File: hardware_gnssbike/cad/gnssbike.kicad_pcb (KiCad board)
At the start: 4 copper layers, 34 x 90 mm, 145 parts, among them J101 HRO TYPE-C-31-M-12, J102 JST SM06B-GHS-TB, J103 JST S4B-ZR-SM4A-TF, J201 Tag-Connect TC2030-NL, J302 Hirose U.FL-R-SMT-1, J401 Hirose FH12-10S-0.5SH(55), J402 HCTL HC-FPC-05-10-5RLTAG, Q401 DMG1012T-7, Q601 DMG1012T-7, Q602 DMG1012T-7, Q603 DMG1012T-7, SW601 XunPu TS-1088R-02026, SW602 XunPu TS-1088R-02026, SW603 XunPu TS-1088R-02026, U101 nPM1300-QEAA, U102 MAX17262REWL, U103 ADP5091ACPZ-2, U104 TPS7A0218PDQN, U201 MinewSemi ME54BS13, U301 u-blox MAX-F10S, U302 TI TXU0204BQAR, U501 MX25R6435F, U502 Bosch BMP585, U503 Bosch BMI270, U504 Memsic MMC5603NJ, U505 TI OPT3001DNPR

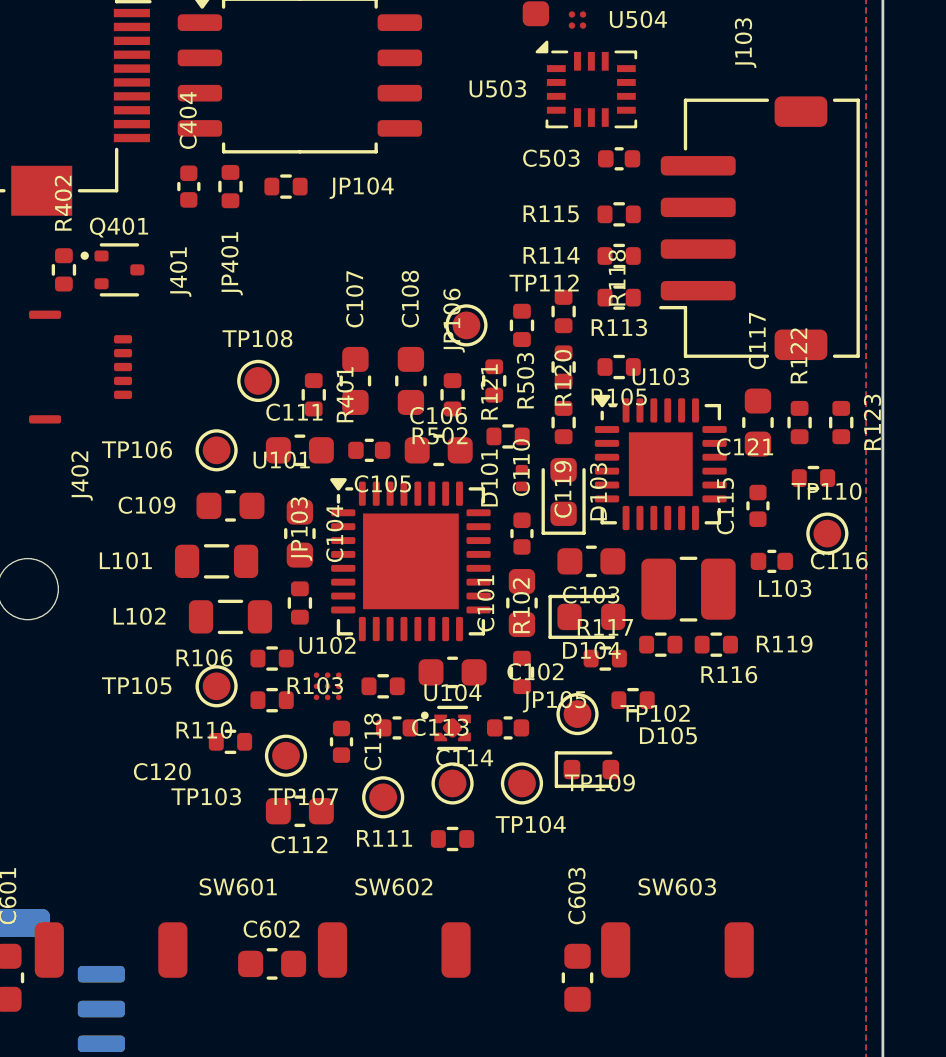
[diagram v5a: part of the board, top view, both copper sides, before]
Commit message: fix(hardware): six pins of the solar harvester were swapped
The second board-killing mistake of the day, and it was caught the same
way as the first: two sources disagreed, and the data sheet decided.

A first reading of the ADP5091 data sheet swapped SIX pins, in two
permutations of three - 2/4/6 (SETHYST, SETSD, TERM) and 7/9/10 (MPPT,
VIN, AGND). It only surfaced because KiCad's own Battery_Management:
ADP5091 symbol disagreed, and because the symbol check had just been
taught to compare pin NAMES and not only numbers. The numbers matched;
the signals did not.

Table 5, pages 8 and 9 of Rev. A (D14145-0-5/17(A)), with Figure 3
confirming side by side, says KiCad is right on all 24. Three
independent readings closed it: the table rebuilt from the geometry of
its columns, the self-consistency of each description - the one for pin
2 says "the SETSD pin", the one for pin 6 says "between SETPG and
SETHYST" - and Figure 3.

What would have gone to copper: the MPPT divider on pin 7, which is
AGND, shorted to analogue ground; the harvester with its 22 uH inductor
and 10 uF capacitor on pin 9, which is MPPT; and ground on pin 10, which
is the input.

The exposed pad is recorded as the data sheet has it: no number at all -
its row in Table 5 has the column empty - and "must be connected to
AGND". The 25 is a CAD convention, which is how KiCad's footprint
numbers it and how its symbol names it, stacked on pin 7.

Beware the preliminary Rev. PrA: its Table 5 swaps 14 and 17 and
contradicts its own Figure 2. It is good for nothing.

With the pinout right, the ADP5091 symbol goes in: 15 KiCad symbols now,
all verified pin number AND pin name.

Verified: check_sch and check_pcb pass, schematic and board agree.
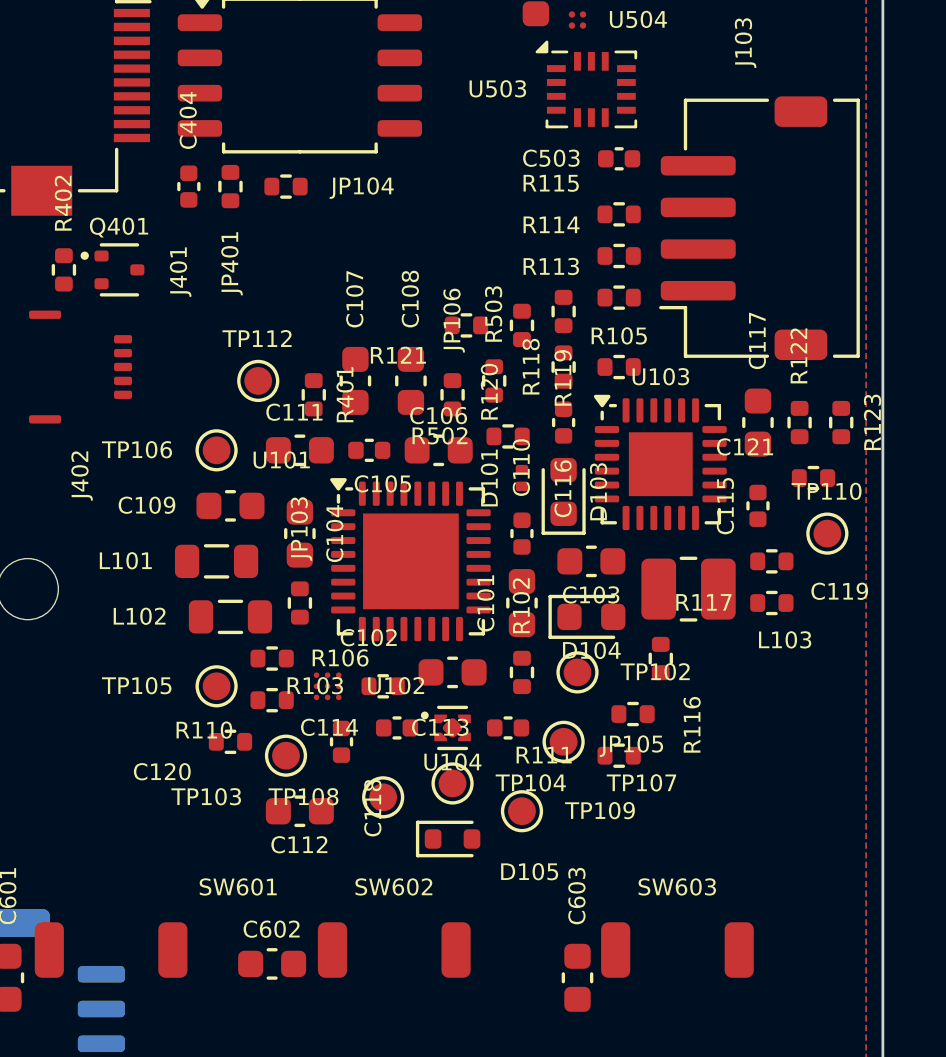
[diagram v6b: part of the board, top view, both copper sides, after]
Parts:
- moved TP108 15.7 mm to (41.0, 77.5)
- moved R119 13.2 mm to (47.5, 60.0), turned to 90 degrees
- moved C116 9.01 mm to (47.5, 64.0), turned to 90 degrees
- moved C119 9.01 mm to (55.0, 69.0), turned to 0 degrees
- moved TP112 7.76 mm to (36.5, 62.5)
- moved TP107 6.80 mm to (47.5, 75.5)
- moved R111 6.71 mm to (49.5, 76.0)
- moved R117 6.32 mm to (55.0, 70.5)
- moved D105 5.59 mm to (43.5, 79.0)
- moved R121 2.00 mm to (44.0, 60.5), turned to 0 degrees
- moved R120 1.58 mm to (46.0, 60.5)
- moved TP102 1.50 mm to (48.0, 73.0)
- moved TP109 1.00 mm to (46.0, 78.0)
- moved JP105 0.50 mm to (50.0, 74.5)
- moved R116 0.50 mm to (51.0, 72.5), turned to 90 degrees
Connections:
- U103 pad 10: GND -> SRC
- U103 pad 2: (no net) -> SETSD
- U103 pad 4: SETSD -> TERM
- U103 pad 6: TERM -> (no net)
- U103 pad 7: MPPT -> GND
- U103 pad 9: SRC -> MPPT
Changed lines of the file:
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@@
 		(at 43.5000 73.0000 0)
 		(property "Reference" "C102"
-			(at 3.0020 0.0000 0)
+			(at -3.0020 -1.2300 0)
 			(layer "F.SilkS")
 			(effects (font (size 0.6 0.6) (thickness 0.12)))
@@
 		(at 41.5000 75.0000 0)
 		(property "Reference" "C114"
-			(at 2.4320 1.1000 0)
+			(at -2.4320 0.0000 0)
 			(layer "F.SilkS")
 			(effects (font (size 0.6 0.6) (thickness 0.12)))
@@
 	(footprint "Capacitor_SMD:C_0402_1005Metric"
 		(layer "F.Cu")
-		(at 55.0000 69.0000 0)
+		(at 47.5000 64.0000 90)
 		(property "Reference" "C116"
-			(at 2.4320 0.0000 0)
+			(at -2.3820 0.0000 90)
 			(layer "F.SilkS")
 			(effects (font (size 0.6 0.6) (thickness 0.12)))
@@
 	)
 	(pad "1" smd roundrect
-		(at -0.48 0)
+		(at -0.48 0 90)
 		(size 0.56 0.62)
 		(layers "F.Cu" "F.Paste" "F.Mask")
@@
 	(pad "2" smd roundrect
 		(net 35 "GND")
-		(at 0.48 0)
+		(at 0.48 0 90)
 		(size 0.56 0.62)
 		(layers "F.Cu" "F.Paste" "F.Mask")
@@
 		(at 39.5000 75.5000 90)
 		(property "Reference" "C118"
-			(at 0.0000 1.1500 90)
+			(at -2.3820 1.1500 90)
 			(layer "F.SilkS")
 			(effects (font (size 0.6 0.6) (thickness 0.12)))
@@
 	(footprint "Resistor_SMD:R_0402_1005Metric"
 		(layer "F.Cu")
-		(at 47.5000 64.0000 90)
+		(at 55.0000 69.0000 0)
 		(property "Reference" "C119"
-			(at -2.4020 0.0000 90)
+			(at 2.4520 1.1000 0)
 			(layer "F.SilkS")
 			(effects (font (size 0.6 0.6) (thickness 0.12)))
@@
 	(pad "1" smd roundrect
 		(net 21 "CBP")
-		(at -0.51 0 90)
+		(at -0.51 0)
 		(size 0.54 0.64)
 		(layers "F.Cu" "F.Paste" "F.Mask")
@@
 	(pad "2" smd roundrect
 		(net 35 "GND")
-		(at 0.51 0 90)
+		(at 0.51 0)
 		(size 0.54 0.64)
 		(layers "F.Cu" "F.Paste" "F.Mask")
@@
 	(footprint "Diode_SMD:D_SOD-523"
 		(layer "F.Cu")
-		(at 48.5000 76.5000 0)
+		(at 43.5000 79.0000 0)
 		(property "Reference" "D105"
-			(at 2.7720 -1.2000 0)
+			(at 2.7720 1.2000 0)
 			(layer "F.SilkS")
 			(effects (font (size 0.6 0.6) (thickness 0.12)))
@@
 	(footprint "Resistor_SMD:R_0402_1005Metric"
 		(layer "F.Cu")
-		(at 50.0000 74.0000 0)
+		(at 50.0000 74.5000 0)
 		(property "Reference" "JP105"
-			(at -2.7700 0.0000 0)
+			(at 0.0000 1.1000 0)
 			(layer "F.SilkS")
 			(effects (font (size 0.6 0.6) (thickness 0.12)))
@@
 		(at 52.0000 70.0000 0)
 		(property "Reference" "L103"
-			(at 3.4720 0.0000 0)
+			(at 3.4720 1.8500 0)
 			(layer "F.SilkS")
 			(effects (font (size 0.6 0.6) (thickness 0.12)))
@@
 		(at 49.5000 62.0000 0)
 		(property "Reference" "R105"
-			(at 0.0000 1.1000 0)
+			(at 0.0000 -1.1000 0)
 			(layer "F.SilkS")
 			(effects (font (size 0.6 0.6) (thickness 0.12)))
@@
 		(at 37.0000 72.5000 0)
 		(property "Reference" "R106"
-			(at -2.4520 0.0000 0)
+			(at 2.4520 0.0000 0)
 			(layer "F.SilkS")
 			(effects (font (size 0.6 0.6) (thickness 0.12)))
@@
 	(footprint "Resistor_SMD:R_0402_1005Metric"
 		(layer "F.Cu")
-		(at 43.5000 79.0000 0)
+		(at 49.5000 76.0000 0)
 		(property "Reference" "R111"
-			(at -2.4520 0.0000 0)
+			(at -2.7020 0.0000 0)
 			(layer "F.SilkS")
 			(effects (font (size 0.6 0.6) (thickness 0.12)))
@@
 		(at 49.5000 59.5000 0)
 		(property "Reference" "R113"
-			(at 0.0000 1.1000 0)
+			(at -2.4520 -1.1000 0)
 			(layer "F.SilkS")
 			(effects (font (size 0.6 0.6) (thickness 0.12)))
@@
 		(at 49.5000 58.0000 0)
 		(property "Reference" "R114"
-			(at -2.4520 0.0000 0)
+			(at -2.4520 -1.1000 0)
 			(layer "F.SilkS")
 			(effects (font (size 0.6 0.6) (thickness 0.12)))
@@
 		(at 49.5000 56.5000 0)
 		(property "Reference" "R115"
-			(at -2.4520 0.0000 0)
+			(at -2.4520 -1.1000 0)
 			(layer "F.SilkS")
 			(effects (font (size 0.6 0.6) (thickness 0.12)))
@@
 	(footprint "Resistor_SMD:R_0402_1005Metric"
 		(layer "F.Cu")
-		(at 51.0000 72.0000 0)
+		(at 51.0000 72.5000 90)
 		(property "Reference" "R116"
-			(at 2.4520 1.1000 0)
+			(at -2.4020 1.1500 90)
 			(layer "F.SilkS")
 			(effects (font (size 0.6 0.6) (thickness 0.12)))
@@
 	(pad "1" smd roundrect
 		(net 58 "MPPT")
-		(at -0.51 0)
+		(at -0.51 0 90)
 		(size 0.54 0.64)
 		(layers "F.Cu" "F.Paste" "F.Mask")
@@
 	(pad "2" smd roundrect
 		(net 35 "GND")
-		(at 0.51 0)
+		(at 0.51 0 90)
 		(size 0.54 0.64)
 		(layers "F.Cu" "F.Paste" "F.Mask")
@@
 	(footprint "Resistor_SMD:R_0402_1005Metric"
 		(layer "F.Cu")
-		(at 49.0000 72.5000 0)
+		(at 55.0000 70.5000 0)
 		(property "Reference" "R117"
-			(at 0.0000 -1.1000 0)
+			(at -2.4520 0.0000 0)
 			(layer "F.SilkS")
 			(effects (font (size 0.6 0.6) (thickness 0.12)))
@@
 		(at 47.5000 62.0000 90)
 		(property "Reference" "R118"
-			(at 3.2020 1.9500 90)
+			(at -0.0000 -1.1500 90)
 			(layer "F.SilkS")
 			(effects (font (size 0.6 0.6) (thickness 0.12)))
@@
 	(footprint "Resistor_SMD:R_0402_1005Metric"
 		(layer "F.Cu")
-		(at 53.0000 72.0000 0)
+		(at 47.5000 60.0000 90)
 		(property "Reference" "R119"
-			(at 2.4520 0.0000 0)
+			(at -2.4020 0.0000 90)
 			(layer "F.SilkS")
 			(effects (font (size 0.6 0.6) (thickness 0.12)))
@@
 	(pad "1" smd roundrect
 		(net 102 "TERM")
-		(at -0.51 0)
+		(at -0.51 0 90)
 		(size 0.54 0.64)
 		(layers "F.Cu" "F.Paste" "F.Mask")
@@
 	(pad "2" smd roundrect
 		(net 35 "GND")
-		(at 0.51 0)
+		(at 0.51 0 90)
 		(size 0.54 0.64)
 		(layers "F.Cu" "F.Paste" "F.Mask")
@@
 	(footprint "Resistor_SMD:R_0402_1005Metric"
 		(layer "F.Cu")
-		(at 47.5000 60.0000 90)
+		(at 46.0000 60.5000 90)
 		(property "Reference" "R120"
-			(at -2.4020 0.0000 90)
+			(at -2.4020 -1.1500 90)
 			(layer "F.SilkS")
 			(effects (font (size 0.6 0.6) (thickness 0.12)))
@@
 	(footprint "Resistor_SMD:R_0402_1005Metric"
 		(layer "F.Cu")
-		(at 46.0000 60.5000 90)
+		(at 44.0000 60.5000 0)
 		(property "Reference" "R121"
-			(at -2.4020 -1.1500 90)
+			(at -2.4520 1.1000 0)
 			(layer "F.SilkS")
 			(effects (font (size 0.6 0.6) (thickness 0.12)))
@@
 	(pad "1" smd roundrect
 		(net 97 "SETSD")
-		(at -0.51 0 90)
+		(at -0.51 0)
 		(size 0.54 0.64)
 		(layers "F.Cu" "F.Paste" "F.Mask")
@@
 	(pad "2" smd roundrect
 		(net 35 "GND")
-		(at 0.51 0 90)
+		(at 0.51 0)
 		(size 0.54 0.64)
 		(layers "F.Cu" "F.Paste" "F.Mask")
@@
 		(at 45.0000 62.5000 90)
 		(property "Reference" "R503"
-			(at 0.0000 1.1500 90)
+			(at 2.4020 -0.0000 90)
 			(layer "F.SilkS")
 			(effects (font (size 0.6 0.6) (thickness 0.12)))
@@
 	(footprint "TestPoint:TestPoint_Pad_D1.0mm"
 		(layer "F.Cu")
-		(at 48.0000 74.5000 0)
+		(at 48.0000 73.0000 0)
 		(property "Reference" "TP102"
 			(at 2.8400 0.0000 0)
@@
 		(at 43.5000 77.0000 0)
 		(property "Reference" "TP104"
-			(at 2.8400 1.5000 0)
+			(at 2.8400 0.0000 0)
 			(layer "F.SilkS")
 			(effects (font (size 0.6 0.6) (thickness 0.12)))
@@
 	(footprint "TestPoint:TestPoint_Pad_D1.0mm"
 		(layer "F.Cu")
-		(at 41.0000 77.5000 0)
+		(at 47.5000 75.5000 0)
 		(property "Reference" "TP107"
-			(at -2.8400 0.0000 0)
+			(at 2.8400 1.5000 0)
 			(layer "F.SilkS")
 			(effects (font (size 0.6 0.6) (thickness 0.12)))
@@
 	(footprint "TestPoint:TestPoint_Pad_D1.0mm"
 		(layer "F.Cu")
-		(at 36.5000 62.5000 0)
+		(at 41.0000 77.5000 0)
 		(property "Reference" "TP108"
-			(at 0.0000 -1.5000 0)
+			(at -2.8400 0.0000 0)
 			(layer "F.SilkS")
 			(effects (font (size 0.6 0.6) (thickness 0.12)))
@@
 	(footprint "TestPoint:TestPoint_Pad_D1.0mm"
 		(layer "F.Cu")
-		(at 46.0000 77.0000 0)
+		(at 46.0000 78.0000 0)
 		(property "Reference" "TP109"
 			(at 2.8400 0.0000 0)
@@
 	(footprint "TestPoint:TestPoint_Pad_D1.0mm"
 		(layer "F.Cu")
-		(at 44.0000 60.5000 0)
+		(at 36.5000 62.5000 0)
 		(property "Reference" "TP112"
-			(at 2.8400 -1.5000 0)
+			(at 0.0000 -1.5000 0)
 			(layer "F.SilkS")
 			(effects (font (size 0.6 0.6) (thickness 0.12)))
@@
 		(at 39.0000 73.5000 0)
 		(property "Reference" "U102"
-			(at 0.0000 -1.4500 0)
+			(at 2.4720 0.0000 0)
 			(layer "F.SilkS")
 			(effects (font (size 0.6 0.6) (thickness 0.12)))
@@
 	)
 	(pad "2" smd roundrect
+		(net 97 "SETSD")
 		(at -1.9375 -0.75)
 		(size 0.875 0.25)
@@
 	)
 	(pad "4" smd roundrect
-		(net 97 "SETSD")
+		(net 102 "TERM")
 		(at -1.9375 0.25)
 		(size 0.875 0.25)
@@
 	)
 	(pad "6" smd roundrect
-		(net 102 "TERM")
 		(at -1.9375 1.25)
 		(size 0.875 0.25)
@@
 	)
 	(pad "7" smd roundrect
-		(net 58 "MPPT")
+		(net 35 "GND")
 		(at -1.25 1.9375)
 		(size 0.25 0.875)
@@
 	)
 	(pad "9" smd roundrect
-		(net 98 "SRC")
+		(net 58 "MPPT")
 		(at -0.25 1.9375)
 		(size 0.25 0.875)
@@
 	)
 	(pad "10" smd roundrect
-		(net 35 "GND")
+		(net 98 "SRC")
 		(at 0.25 1.9375)
 		(size 0.25 0.875)
@@
 		(at 43.5000 75.0000 0)
 		(property "Reference" "U104"
-			(at 0.0000 -1.2500 0)
+			(at 0.0000 1.2500 0)
 			(layer "F.SilkS")
 			(effects (font (size 0.6 0.6) (thickness 0.12)))

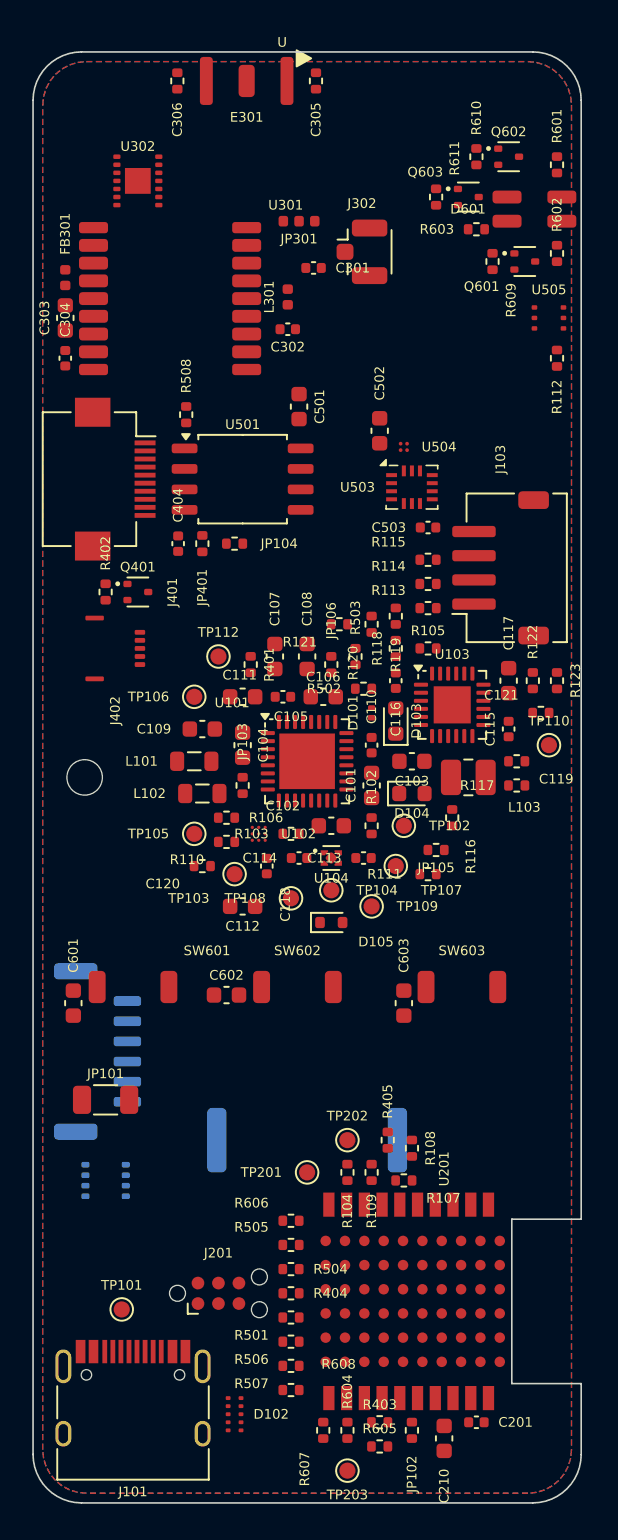
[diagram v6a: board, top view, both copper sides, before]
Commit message: feat(hardware): route the board again and cut the deliverables
With the harvester's six pins fixed, the debug connector's RESET moved
and fifteen symbols coming from KiCad's library, everything downstream
had to be made again.

Board: 966 segments, 450 vias, 151 connections routed, the KiCad DRC
with 0 violations and 0 unconnected items, and 18 of the datasheet rules
measured and met. The one that is not is US1, the USB differential pair,
which still needs hand finishing at 0,352 mm.

Schematic: 6 sheets, the ERC accusing no error outside the four that are
listed with their reason.

Out of it: the schematic PDF, the board layer by layer, the assembly
drawing with 110 of 144 references on leader lines, the four rendered
views, and a GLB of 38 MB. The GLB is the one that carries the
manufacturer's STEP models - the USB-C, the JST ZH, the FPC and the
LFCSP - because KiCad's GLB export reads STEP and never VRML, which is
what this project's own renderer draws.
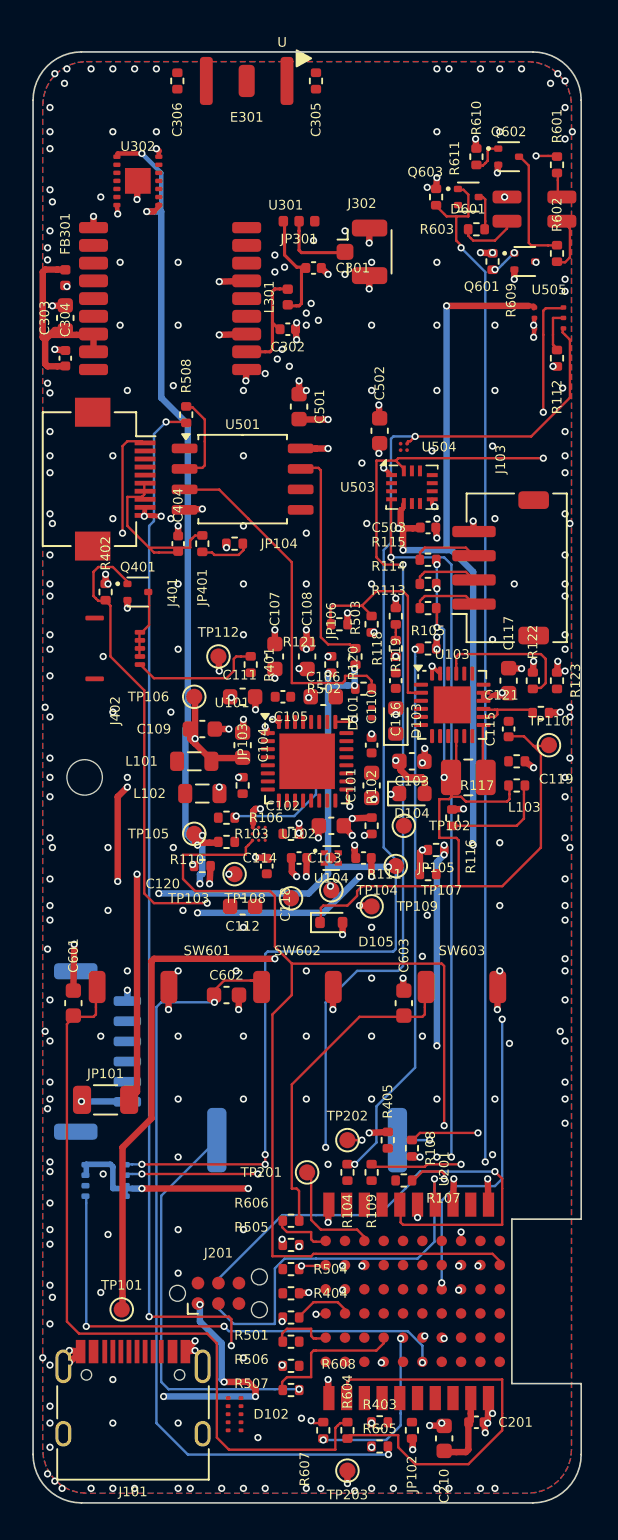
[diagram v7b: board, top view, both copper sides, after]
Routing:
- net 3V0: track 0.00 -> 261.3 mm, vias 0 -> 24
- net 3V0_SENS: track 0.00 -> 113.1 mm, vias 0 -> 12
- net SENS_SDA: track 0.00 -> 92.7 mm, vias 0 -> 7
- net SENS_SCL: track 0.00 -> 90.7 mm, vias 0 -> 6
- net DISP_SCK: track 0.00 -> 87.4 mm, vias 0 -> 2
- net RGB_B: track 0.00 -> 79.6 mm, vias 0 -> 3
- net PWR_SDA: track 0.00 -> 75.8 mm, vias 0 -> 2
- net BL_PWM: track 0.00 -> 73.3 mm, vias 0 -> 3
- net NOR_MISO: track 0.00 -> 72.5 mm, vias 0 -> 4
- net GND: track 0.00 -> 67.2 mm, vias 0 -> 312
- net SD3V0: track 0.00 -> 65.8 mm, vias 0 -> 6
- net VSYS: track 0.00 -> 63.2 mm, vias 0 -> 4
- net IMU_INT: track 0.00 -> 57.4 mm, vias 0 -> 3
- net SRC: track 0.00 -> 57.1 mm, vias 0 -> 4
- net 1V8: track 0.00 -> 50.7 mm, vias 0 -> 3
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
